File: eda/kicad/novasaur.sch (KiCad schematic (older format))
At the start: 28 parts, among them J9 RAM, SW1 RESET, U1 74F86, U10 74F574, U11 74F574, U12 ATF16V8, U2 74F08, U3 74F32, U4 74ALS139, U5 74ALS139, U6 74F157, U7 74F175, U8 74F574, U9 74F138, X1 33M

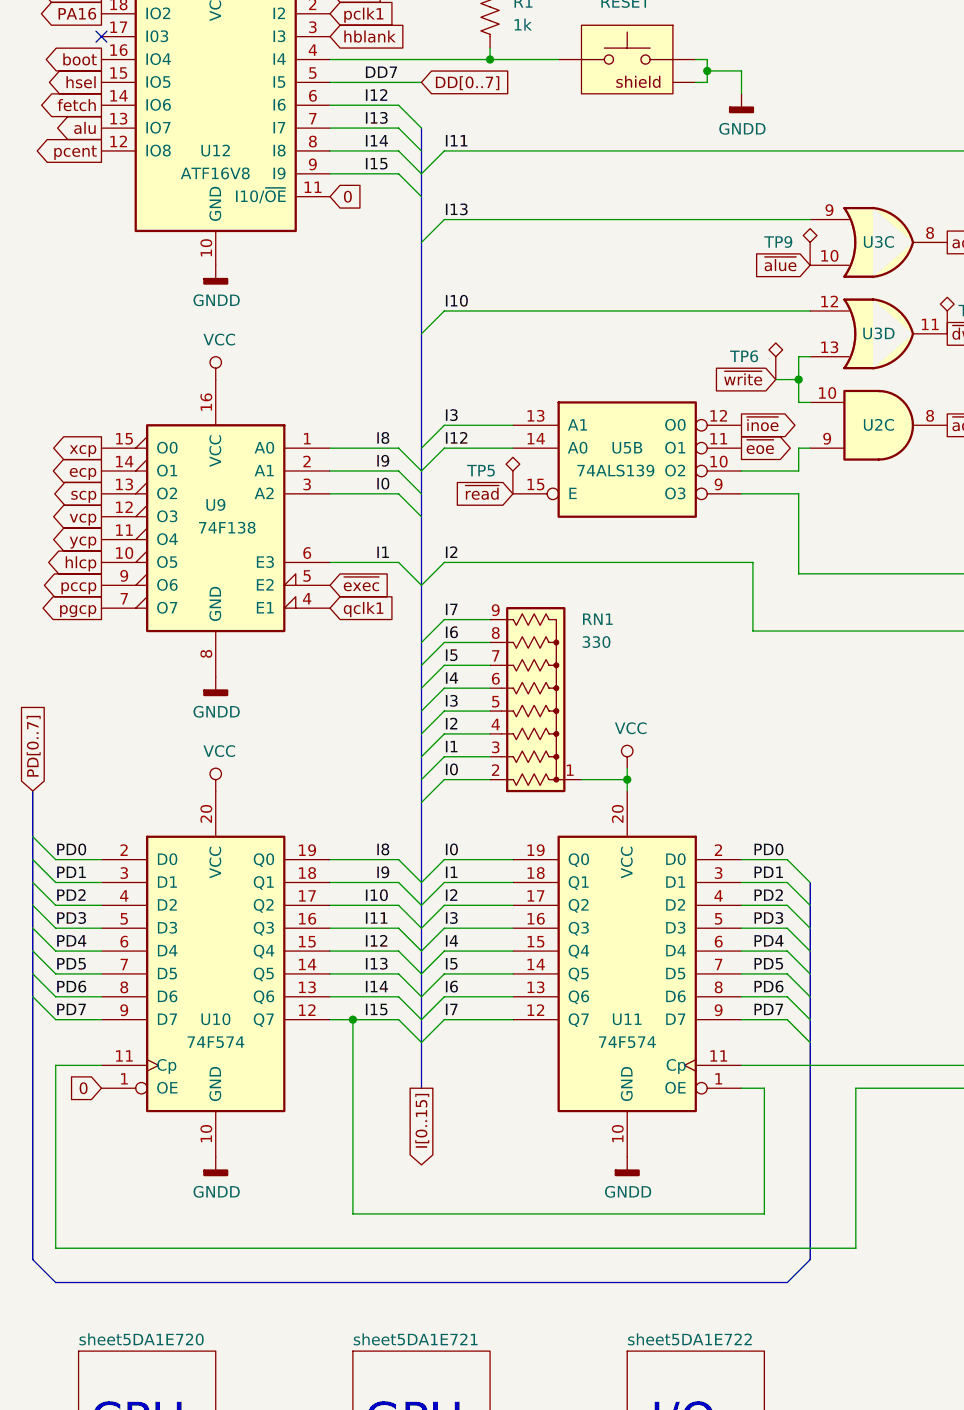
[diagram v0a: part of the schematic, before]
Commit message: build out, fix bugs Build out the initial HAL VM code to generate video timing. Not quite working yet, but lots of bugs fixed with assembler and code
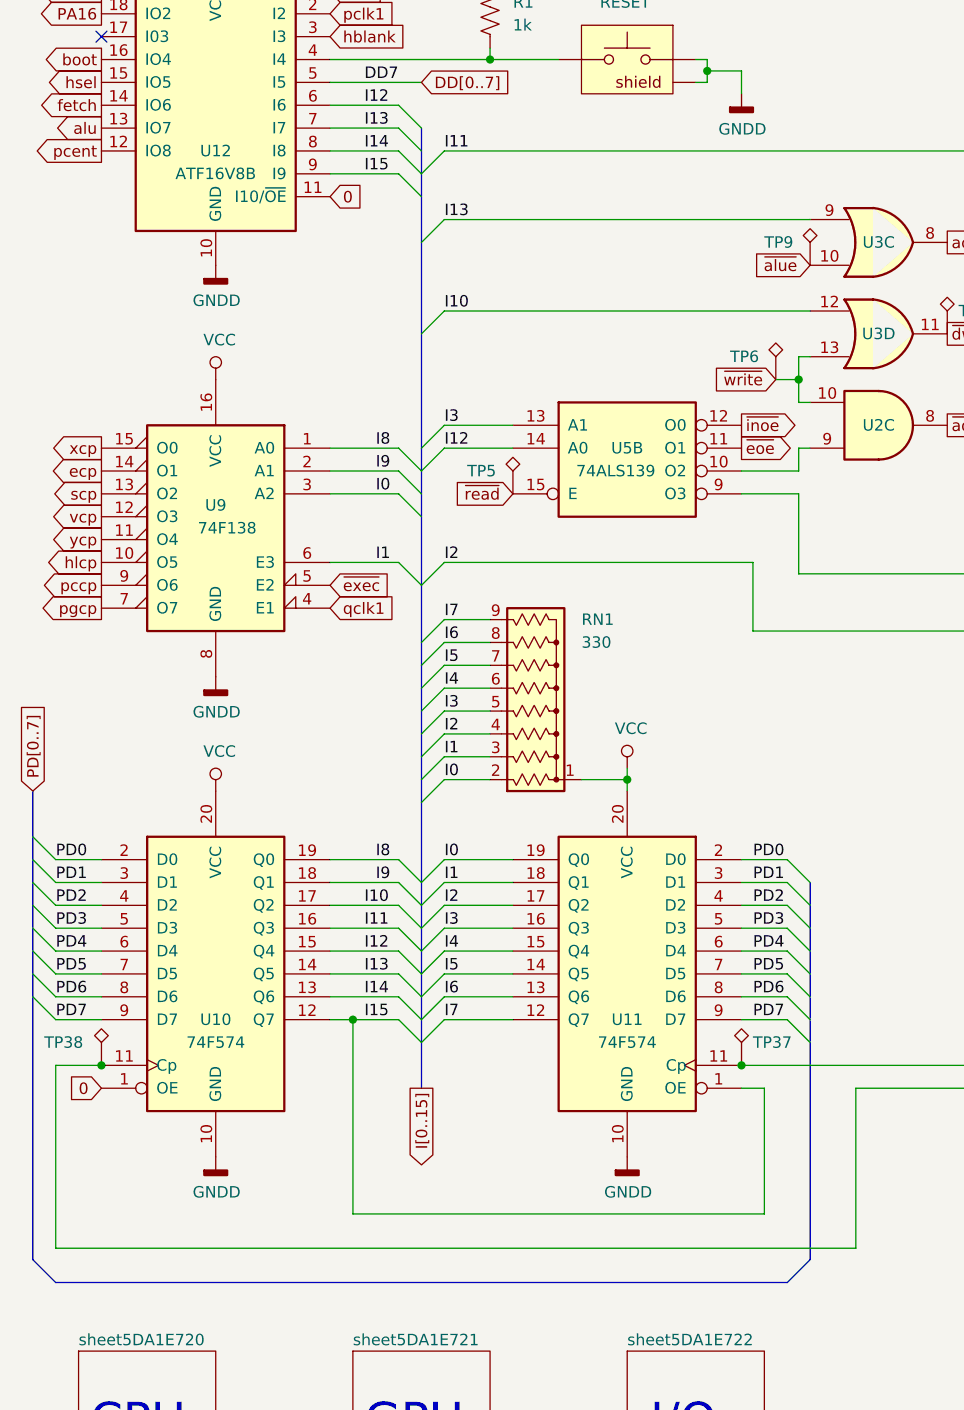
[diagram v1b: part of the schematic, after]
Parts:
- added TP37: ILCP, TestPoint:TestPoint_Pad_1.0x1.0mm, symbol Connector:TestPoint_Alt
- added TP38: IHCP, TestPoint:TestPoint_Pad_1.0x1.0mm, symbol Connector:TestPoint_Alt
- U12: value ATF16V8 -> ATF16V8B
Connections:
- net at U11.11 (Cp), U4.10 (O2): now also TP37.1
- net at U10.11 (Cp), U4.9 (O3): now also TP38.1
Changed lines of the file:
@@
 Sheet 1 4
 Title "Novasaur TTL Minicomputer"
-Date "2020-02-15"
+Date "2020-02-20"
 Rev "1.5"
 Comp ""
@@
 	2350 1700 2650 1700
 NoConn ~ 1350 1400
-Wire Wire Line
-	1350 5900 1150 5900
-Wire Wire Line
-	1150 5900 1150 6700
 Entry Bus Bus
 	4350 6850 4450 6750
@@
 AR Path="/5DA1E80A" Ref="U12"  Part="1"
 F 0 "U12" H 1850 1500 50  0000 C CNN
-F 1 "ATF16V8" H 1850 1400 50  0000 C CNN
+F 1 "ATF16V8B" H 1850 1400 50  0000 C CNN
 F 2 "Package_DIP:DIP-20_W7.62mm_Socket_LongPads" H 1850 1700 50  0001 C CNN
 F 3 "" H 1850 1700 50  0001 C CNN
@@
 	4650 6000 5600 6000
 Wire Wire Line
-	5600 5900 4150 5900
-Wire Wire Line
 	7800 5500 7900 5500
 Connection ~ 7900 5500
@@
 Text GLabel 6850 2900 0    50   Input ~ 0
 1
+$Comp
+L Connector:TestPoint_Alt TP38
+U 1 1 5E51CAB2
+P 1350 5900
+AR Path="/5E51CAB2" Ref="TP38"  Part="1"
+AR Path="/5DA1E9BA/5E51CAB2" Ref="TP?"  Part="1"
+AR Path="/5DA1E9BD/5E51CAB2" Ref="TP?"  Part="1"
+AR Path="/5DA1E9C0/5E51CAB2" Ref="TP?"  Part="1"
+F 0 "TP38" H 1100 6000 50  0000 L CNN
+F 1 "IHCP" H 1100 6050 50  0001 L CNN
+F 2 "TestPoint:TestPoint_Pad_1.0x1.0mm" H 1550 5900 50  0001 C CNN
+F 3 "~" H 1550 5900 50  0001 C CNN
+	1    1350 5900
+	1    0    0    -1
+$EndComp
+Wire Wire Line
+	1150 6700 1150 5900
+Wire Wire Line
+	1150 5900 1350 5900
+Connection ~ 1350 5900
+Wire Wire Line
+	5600 5900 4150 5900
+Connection ~ 4150 5900
+$Comp
+L Connector:TestPoint_Alt TP37
+U 1 1 5E514E07
+P 4150 5900
+AR Path="/5E514E07" Ref="TP37"  Part="1"
+AR Path="/5DA1E9BA/5E514E07" Ref="TP?"  Part="1"
+AR Path="/5DA1E9BD/5E514E07" Ref="TP?"  Part="1"
+AR Path="/5DA1E9C0/5E514E07" Ref="TP?"  Part="1"
+F 0 "TP37" H 4200 6000 50  0000 L CNN
+F 1 "ILCP" H 3900 6050 50  0001 L CNN
+F 2 "TestPoint:TestPoint_Pad_1.0x1.0mm" H 4350 5900 50  0001 C CNN
+F 3 "~" H 4350 5900 50  0001 C CNN
+	1    4150 5900
+	1    0    0    -1
+$EndComp
 Wire Bus Line
 	4450 5100 4450 6750

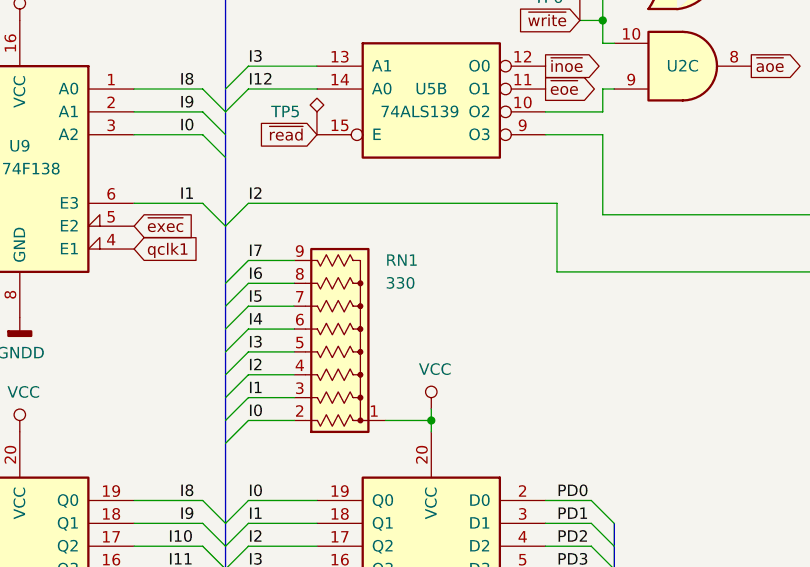
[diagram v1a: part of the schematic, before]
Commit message: final rev5 update before removing buck reg
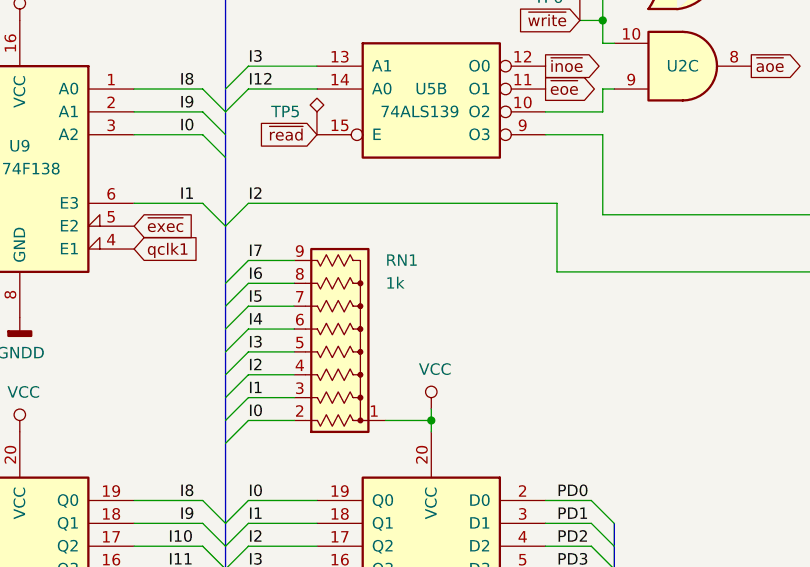
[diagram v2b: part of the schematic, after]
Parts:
- RN1: value 330 -> 1k
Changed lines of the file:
@@
 AR Path="/5DA1E820" Ref="RN1"  Part="1"
 F 0 "RN1" V 3550 4450 50  0000 L CNN
-F 1 "330" V 3450 4450 50  0000 L CNN
+F 1 "1k" V 3450 4450 50  0000 L CNN
 F 2 "Resistor_THT:R_Array_SIP9" V 3725 4250 50  0001 C CNN
 F 3 "http://www.vishay.com/docs/31509/csc.pdf" H 3250 4250 50  0001 C CNN

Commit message: rev 1.6 schematic
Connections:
- net ~reset: now reaches R1.2, SW1.2, U12.4 (I4)
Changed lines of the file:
@@
 Sheet 1 4
 Title "Novasaur TTL Minicomputer"
-Date "2020-03-01"
-Rev "1.5"
+Date "2020-03-08"
+Rev "1.6"
 Comp ""
 Comment1 "(c) A J Hewitt 2020"
@@
 Connection ~ 3050 1500
 Wire Wire Line
-	3050 1500 3350 1500
-Wire Wire Line
-	2350 1500 3050 1500
+	2350 1500 2850 1500
 Wire Wire Line
 	4200 3700 4200 4000
@@
 	1    0    0    -1
 $EndComp
+Text GLabel 2850 1400 1    50   Input ~ 0
+~reset
+Wire Wire Line
+	3050 1500 3350 1500
+Wire Wire Line
+	2850 1400 2850 1500
+Connection ~ 2850 1500
+Wire Wire Line
+	2850 1500 3050 1500
 Wire Bus Line
 	4450 5100 4450 6750

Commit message: rename P reg to T
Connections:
- net ~poe renamed ~toe
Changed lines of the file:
@@
 Sheet 1 4
 Title "Novasaur TTL Minicomputer"
-Date "2020-03-08"
+Date "2020-03-29"
 Rev "1.6"
 Comp ""
@@
 ~xoe
 Text GLabel 9300 2200 2    50   Output ~ 0
-~poe
+~toe
 $Comp
 L 74xx:74LS574 U?

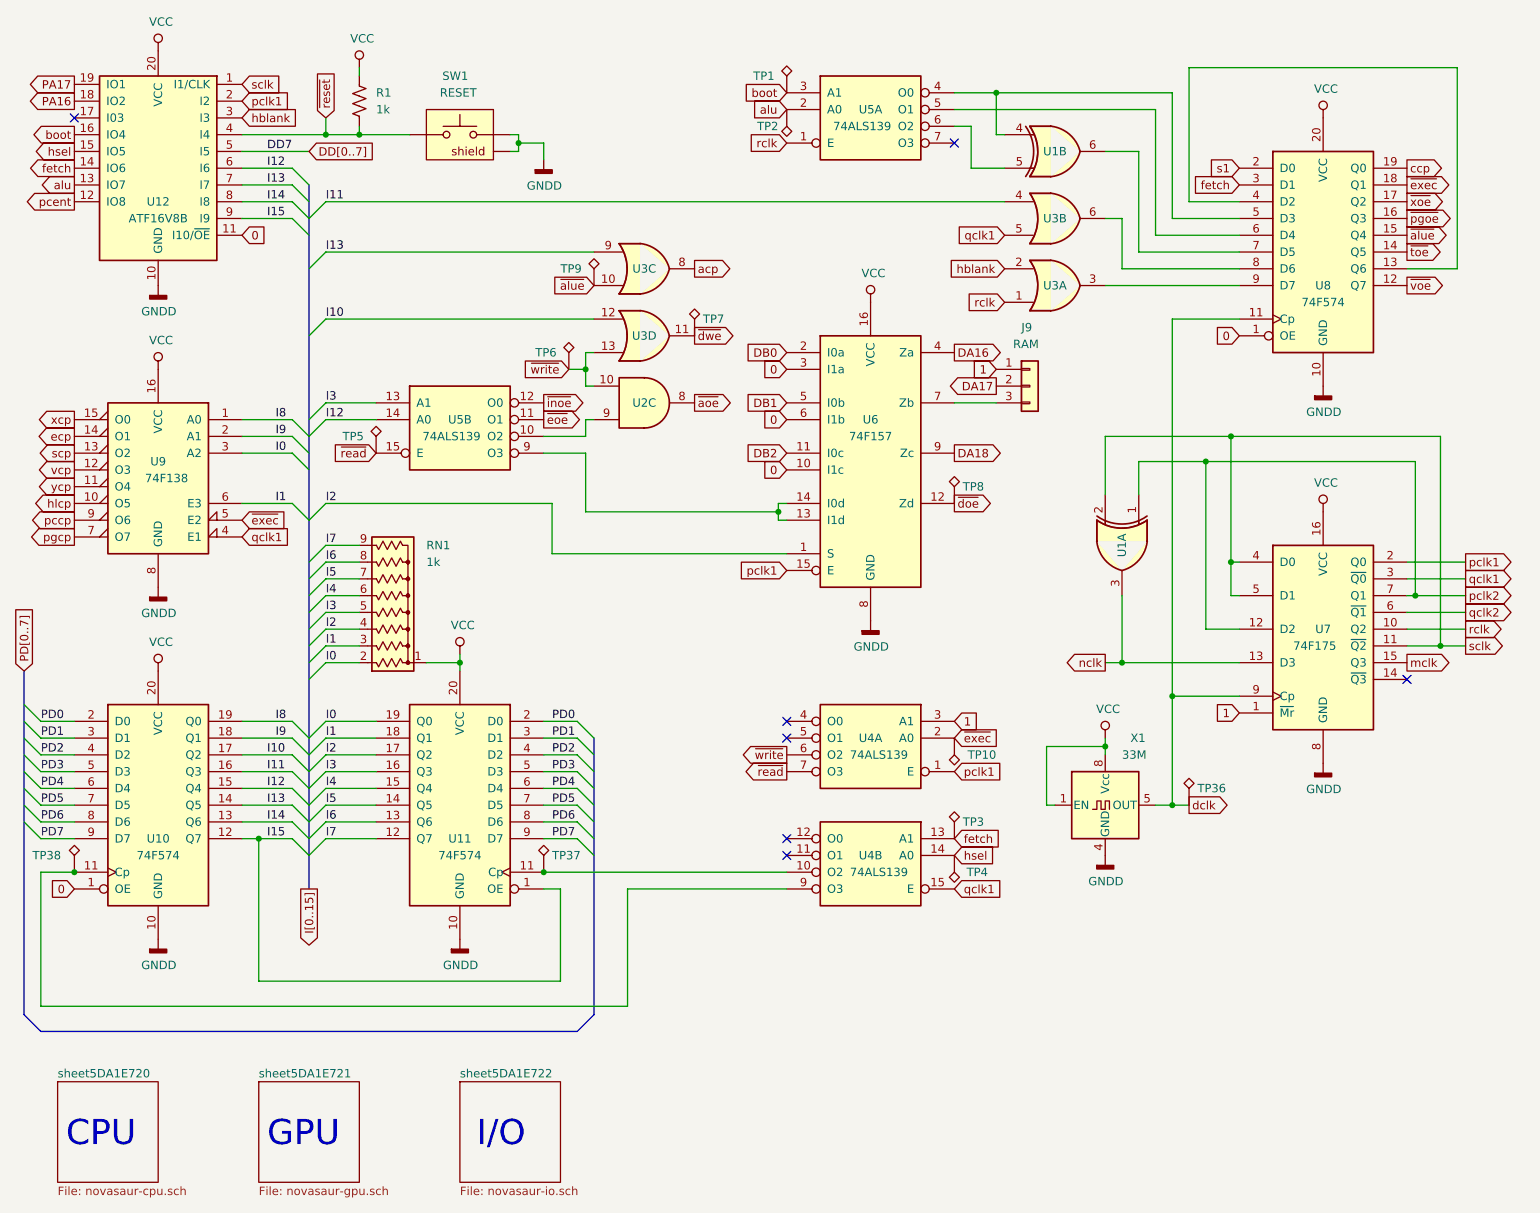
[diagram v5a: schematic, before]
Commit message: add video headers
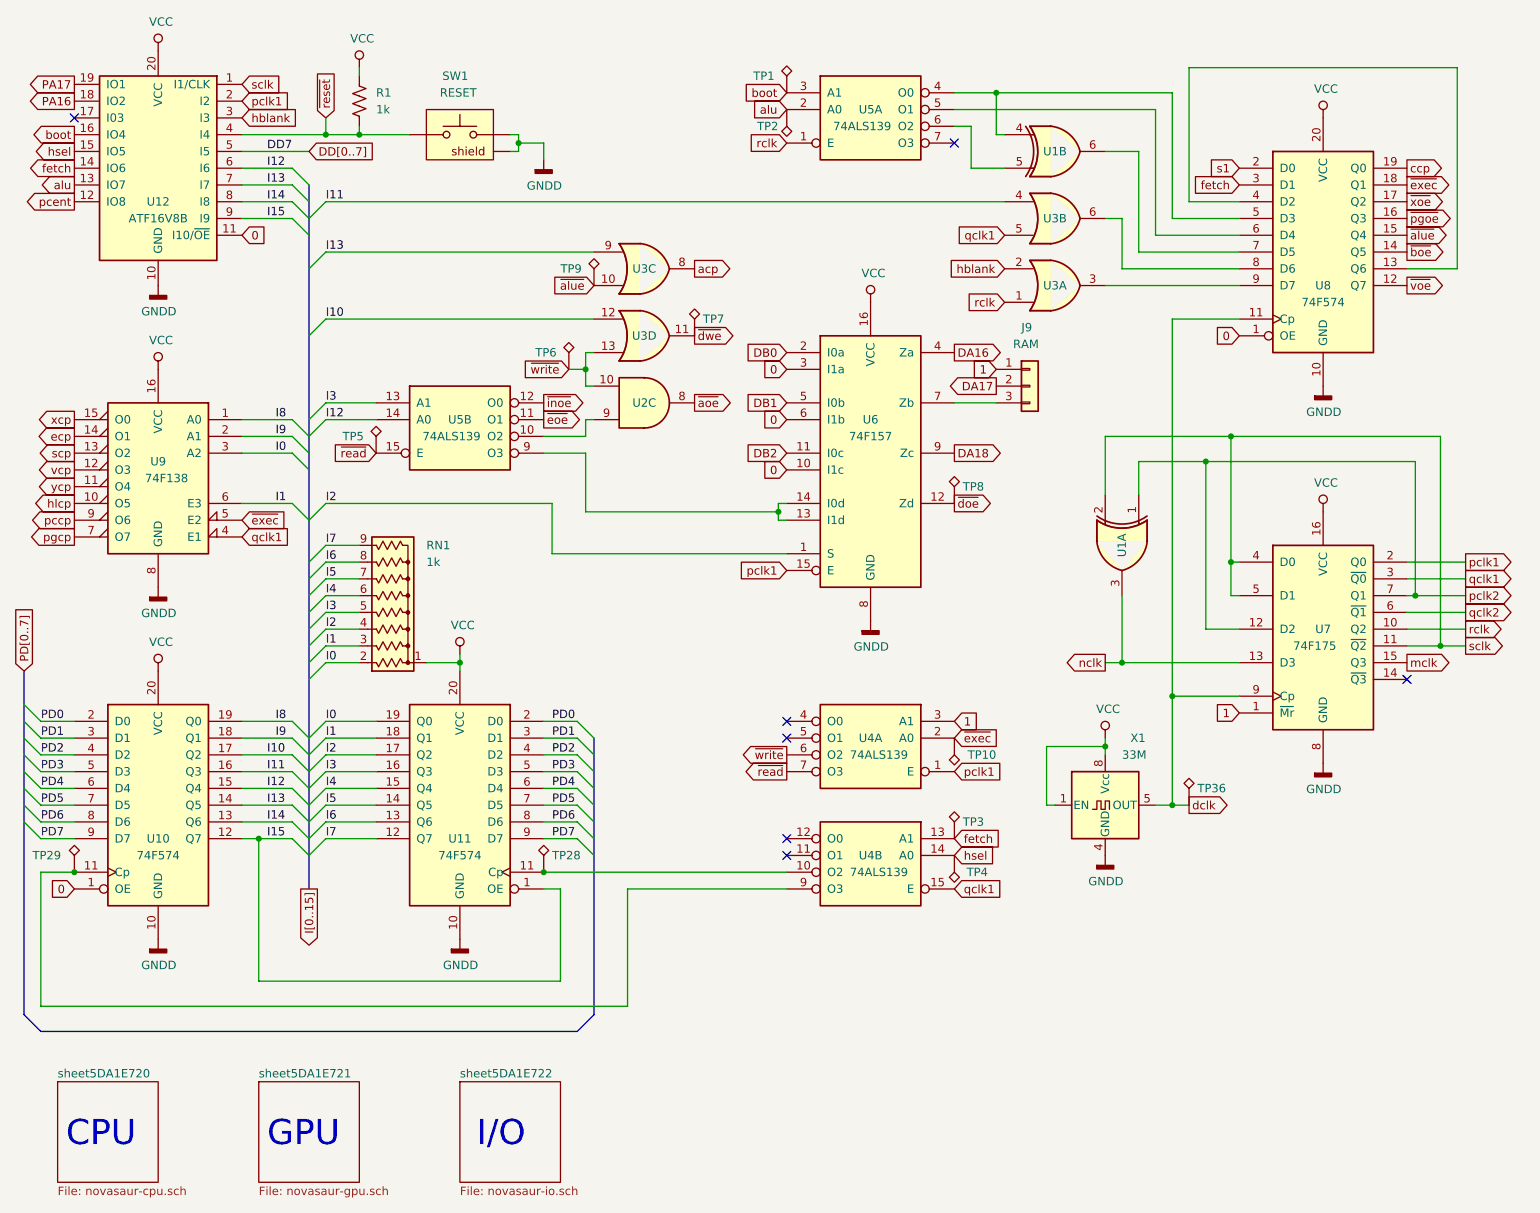
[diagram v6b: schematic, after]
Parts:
- renumbered TP37 to TP28, TP38 to TP29
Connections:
- net ~toe renamed ~boe
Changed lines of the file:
@@
 encoding utf-8
 Sheet 1 4
-Title "Novasaur TTL Minicomputer"
-Date "2020-03-29"
+Title "Novasaur Retrocomputer"
+Date "2020-03-31"
 Rev "1.6"
 Comp ""
@@
 ~xoe
 Text GLabel 9300 2200 2    50   Output ~ 0
-~toe
+~boe
 $Comp
 L 74xx:74LS574 U?
@@
 1
 $Comp
-L Connector:TestPoint_Alt TP38
+L Connector:TestPoint_Alt TP29
 U 1 1 5E51CAB2
 P 1350 5900
-AR Path="/5E51CAB2" Ref="TP38"  Part="1"
+AR Path="/5E51CAB2" Ref="TP29"  Part="1"
 AR Path="/5DA1E9BA/5E51CAB2" Ref="TP?"  Part="1"
 AR Path="/5DA1E9BD/5E51CAB2" Ref="TP?"  Part="1"
 AR Path="/5DA1E9C0/5E51CAB2" Ref="TP?"  Part="1"
-F 0 "TP38" H 1100 6000 50  0000 L CNN
+F 0 "TP29" H 1100 6000 50  0000 L CNN
 F 1 "IHCP" H 1100 6050 50  0001 L CNN
 F 2 "TestPoint:TestPoint_Pad_1.0x1.0mm" H 1550 5900 50  0001 C CNN
@@
 	5600 5900 4150 5900
 Connection ~ 4150 5900
-$Comp
-L Connector:TestPoint_Alt TP37
-U 1 1 5E514E07
-P 4150 5900
-AR Path="/5E514E07" Ref="TP37"  Part="1"
-AR Path="/5DA1E9BA/5E514E07" Ref="TP?"  Part="1"
-AR Path="/5DA1E9BD/5E514E07" Ref="TP?"  Part="1"
-AR Path="/5DA1E9C0/5E514E07" Ref="TP?"  Part="1"
-F 0 "TP37" H 4200 6000 50  0000 L CNN
-F 1 "ILCP" H 3900 6050 50  0001 L CNN
-F 2 "TestPoint:TestPoint_Pad_1.0x1.0mm" H 4350 5900 50  0001 C CNN
-F 3 "~" H 4350 5900 50  0001 C CNN
-	1    4150 5900
-	1    0    0    -1
-$EndComp
 Text GLabel 2850 1400 1    50   Input ~ 0
 ~reset
@@
 Wire Bus Line
 	2750 1800 2750 6000
+$Comp
+L Connector:TestPoint_Alt TP28
+U 1 1 5E514E07
+P 4150 5900
+AR Path="/5E514E07" Ref="TP28"  Part="1"
+AR Path="/5DA1E9BA/5E514E07" Ref="TP?"  Part="1"
+AR Path="/5DA1E9BD/5E514E07" Ref="TP?"  Part="1"
+AR Path="/5DA1E9C0/5E514E07" Ref="TP?"  Part="1"
+F 0 "TP28" H 4200 6000 50  0000 L CNN
+F 1 "ILCP" H 3900 6050 50  0001 L CNN
+F 2 "TestPoint:TestPoint_Pad_1.0x1.0mm" H 4350 5900 50  0001 C CNN
+F 3 "~" H 4350 5900 50  0001 C CNN
+	1    4150 5900
+	1    0    0    -1
+$EndComp
 $EndSCHEMATC
